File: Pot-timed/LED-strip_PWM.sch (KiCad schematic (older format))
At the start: 14 parts, among them IC1 ATTINY13A-MM, P1 CONN_2, P2 CONN_2, T1 AO3400, U1 MCP1804-SOT23-5

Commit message: Pot-timed: Attiny13 MLF10 (Unobtanium) --> MLF20.
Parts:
- removed IC1: ATTINY13A-MM, QFN/MLF10, symbol ATTINY13A-MM
- added IC1: ATTINY13-M, QFN/MLF20, symbol ATTINY13-M
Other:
- note added: "(MLF-20)"
- note removed: "(MLF-10)"
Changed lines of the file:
@@
-$EndComp
-$Comp
-L ATTINY13A-MM IC1
-U 1 1 519FBED0
-P 1400 800
-F 0 "IC1" H 1500 850 60  0000 C CNN
-F 1 "ATTINY13A-MM" H 2700 50  60  0000 C CNN
-F 2 "QFN/MLF10" H 1700 50  60  0001 C CNN
-F 3 "~" H 1400 800 60  0000 C CNN
-	1    1400 800
-	1    0    0    -1
 $EndComp
 $Comp
@@
 POT1
 Text Notes 2700 775  0    39   ~ 0
-(MLF-10)
+(MLF-20)
 Text Label 950  1300 2    60   ~ 0
 POT2
@@
 Wire Notes Line
 	7300 2000 6000 2000
+$Comp
+L ATTINY13-M IC1
+U 1 1 519FFF57
+P 1400 800
+F 0 "IC1" H 1500 850 60  0000 C CNN
+F 1 "ATTINY13-M" H 2700 50  60  0000 C CNN
+F 2 "QFN/MLF20" H 1700 50  60  0001 C CNN
+F 3 "~" H 1400 800 60  0000 C CNN
+	1    1400 800
+	1    0    0    -1
+$EndComp
 $EndSCHEMATC

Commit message: Pot-timed: Found Attiny13 MLF10 at digikey...
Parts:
- removed IC1: ATTINY13-M, QFN/MLF20, symbol ATTINY13-M
- added IC1: ATTINY13A-MM, QFN/MLF10, symbol ATTINY13A-MM
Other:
- note added: "(MLF-10)"
- note removed: "(MLF-20)"
- moved on the sheet: RV1
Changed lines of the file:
@@
 POT1
 Text Notes 2700 775  0    39   ~ 0
-(MLF-20)
+(MLF-10)
 Text Label 950  1300 2    60   ~ 0
 POT2
@@
 F 3 "~" H 6450 2550 60  0000 C CNN
 	1    6450 2550
-	0    -1   -1   0
+	0    1    1    0
 $EndComp
 $Comp
@@
 	6800 2850 6800 2900
 Connection ~ 6800 2850
-Text Label 6250 2550 2    60   ~ 0
+Text Label 6650 2550 3    60   ~ 0
 POT1
-Text Label 6900 2550 2    60   ~ 0
+Text Label 6900 2550 1    60   ~ 0
 POT2
 Wire Wire Line
 	6900 2550 6950 2550
-Wire Wire Line
-	6250 2550 6300 2550
 Wire Notes Line
 	6000 2000 6000 3000
@@
 	7300 2000 6000 2000
 $Comp
-L ATTINY13-M IC1
-U 1 1 519FFF57
+L ATTINY13A-MM IC1
+U 1 1 51A021E9
 P 1400 800
 F 0 "IC1" H 1500 850 60  0000 C CNN
-F 1 "ATTINY13-M" H 2700 50  60  0000 C CNN
-F 2 "QFN/MLF20" H 1700 50  60  0001 C CNN
+F 1 "ATTINY13A-MM" H 2700 50  60  0000 C CNN
+F 2 "QFN/MLF10" H 1700 50  60  0001 C CNN
 F 3 "~" H 1400 800 60  0000 C CNN
 	1    1400 800
 	1    0    0    -1
 $EndComp
+Wire Wire Line
+	6600 2550 6650 2550
 $EndSCHEMATC

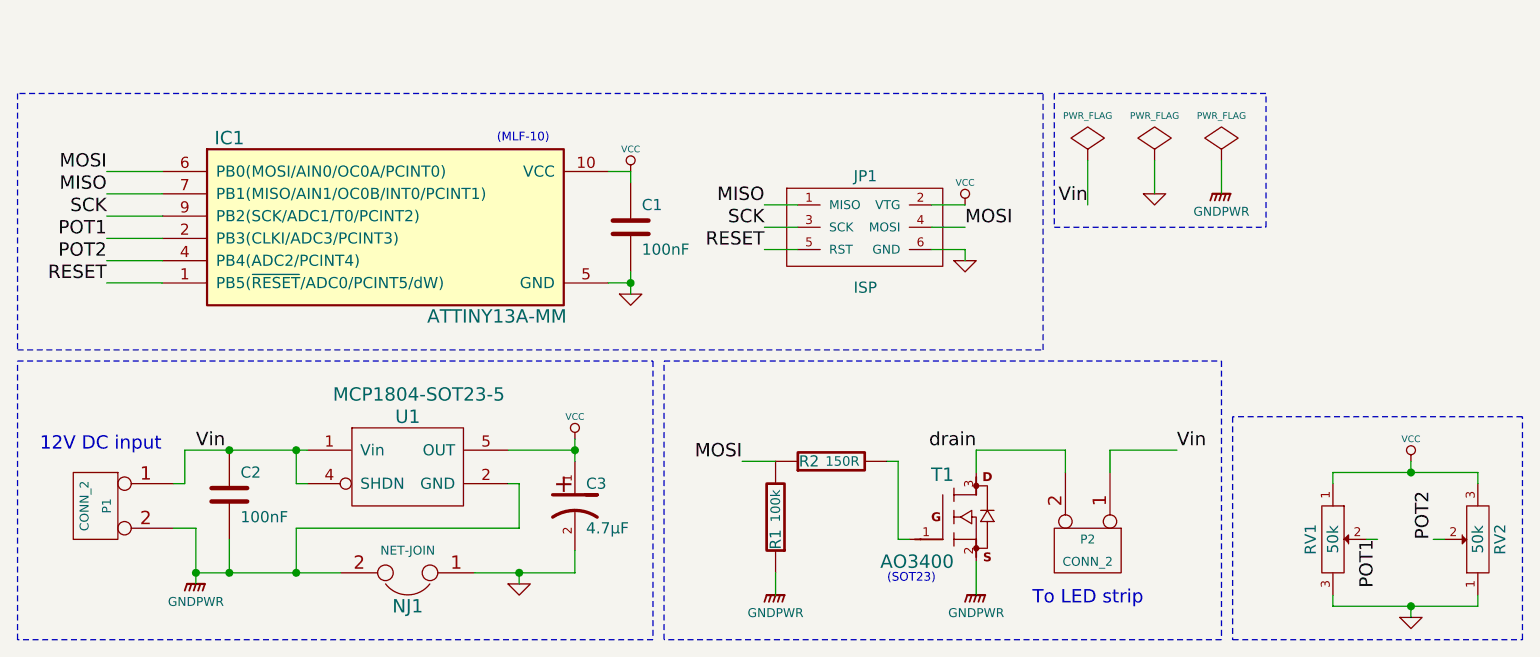
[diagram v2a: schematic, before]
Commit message: Changed to custom attiny13 schematic symbol + footprint.
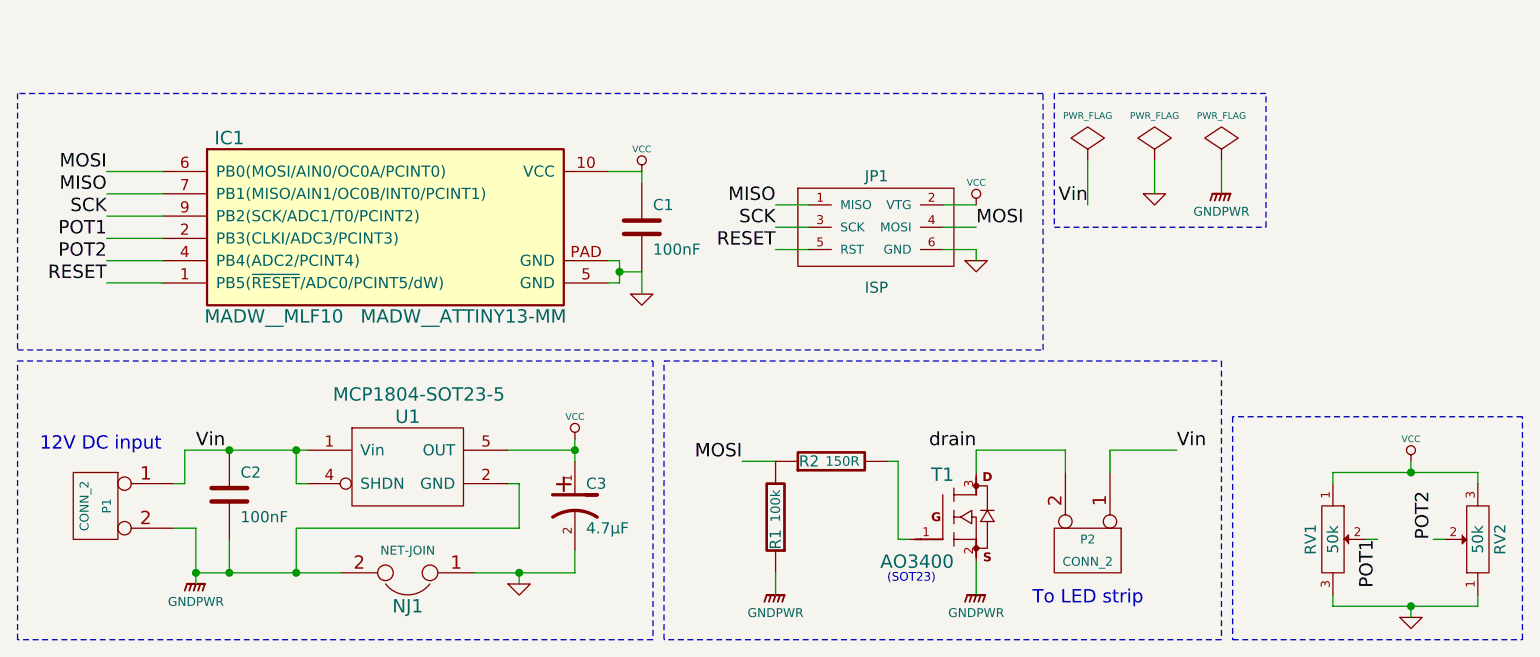
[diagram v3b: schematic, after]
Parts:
- removed IC1: ATTINY13A-MM, QFN/MLF10, symbol ATTINY13A-MM
- added IC1: MADW__ATTINY13-MM, MADW__MLF10, symbol MADW__ATTINY13-MM
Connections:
- net GND: now also IC1.5 (GND), IC1.PAD (GND)
- net MISO: now also IC1.7 (PB1(MISO/AIN1/OC0B/INT0/PCINT1))
- net MOSI: now also IC1.6 (PB0(MOSI/AIN0/OC0A/PCINT0))
- net POT1: now also IC1.2 (PB3(CLKI/ADC3/PCINT3))
- net POT2: now also IC1.4 (PB4(ADC2/PCINT4))
- net RESET: now also IC1.1 (PB5(~RESET~/ADC0/PCINT5/dW))
- net SCK: now also IC1.9 (PB2(SCK/ADC1/T0/PCINT2))
- net VCC: now also IC1.10 (VCC)
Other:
- note removed: "(MLF-10)"
- moved on the sheet: C1, JP1
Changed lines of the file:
@@
-$EndComp
-$Comp
-L C C1
-U 1 1 4F76EBA8
-P 3300 1150
-F 0 "C1" H 3350 1250 50  0000 L CNN
-F 1 "100nF" H 3350 1050 50  0000 L CNN
-F 2 "" H 3300 1150 60  0001 C CNN
-F 3 "" H 3300 1150 60  0001 C CNN
-	1    3300 1150
-	1    0    0    -1
 $EndComp
 $Comp
@@
 L VCC #PWR02
 U 1 1 4F6EE887
-P 3300 900
-F 0 "#PWR02" H 3300 1000 30  0001 C CNN
-F 1 "VCC" H 3300 1000 30  0000 C CNN
-F 2 "" H 3300 900 60  0001 C CNN
-F 3 "" H 3300 900 60  0001 C CNN
-	1    3300 900
+P 3350 900
+F 0 "#PWR02" H 3350 1000 30  0001 C CNN
+F 1 "VCC" H 3350 1000 30  0000 C CNN
+F 2 "" H 3350 900 60  0001 C CNN
+F 3 "" H 3350 900 60  0001 C CNN
+	1    3350 900
 	1    0    0    -1
 $EndComp
@@
 L GND #PWR03
 U 1 1 4F6EE882
-P 3300 1450
-F 0 "#PWR03" H 3300 1450 30  0001 C CNN
-F 1 "GND" H 3300 1380 30  0001 C CNN
-F 2 "" H 3300 1450 60  0001 C CNN
-F 3 "" H 3300 1450 60  0001 C CNN
-	1    3300 1450
+P 3350 1450
+F 0 "#PWR03" H 3350 1450 30  0001 C CNN
+F 1 "GND" H 3350 1380 30  0001 C CNN
+F 2 "" H 3350 1450 60  0001 C CNN
+F 3 "" H 3350 1450 60  0001 C CNN
+	1    3350 1450
 	1    0    0    -1
 $EndComp
@@
 L GND #PWR04
 U 1 1 4F6EE81E
-P 4800 1300
-F 0 "#PWR04" H 4800 1300 30  0001 C CNN
-F 1 "GND" H 4800 1230 30  0001 C CNN
-F 2 "" H 4800 1300 60  0001 C CNN
-F 3 "" H 4800 1300 60  0001 C CNN
-	1    4800 1300
-	1    0    0    -1
-$EndComp
-Text Label 4800 1150 0    60   ~ 0
+P 4850 1300
+F 0 "#PWR04" H 4850 1300 30  0001 C CNN
+F 1 "GND" H 4850 1230 30  0001 C CNN
+F 2 "" H 4850 1300 60  0001 C CNN
+F 3 "" H 4850 1300 60  0001 C CNN
+	1    4850 1300
+	1    0    0    -1
+$EndComp
+Text Label 4850 1150 0    60   ~ 0
 MOSI
 $Comp
 L VCC #PWR05
 U 1 1 4F6EE80A
-P 4800 1050
-F 0 "#PWR05" H 4800 1150 30  0001 C CNN
-F 1 "VCC" H 4800 1150 30  0000 C CNN
-F 2 "" H 4800 1050 60  0001 C CNN
-F 3 "" H 4800 1050 60  0001 C CNN
-	1    4800 1050
-	1    0    0    -1
-$EndComp
-Text Label 3900 1250 2    60   ~ 0
+P 4850 1050
+F 0 "#PWR05" H 4850 1150 30  0001 C CNN
+F 1 "VCC" H 4850 1150 30  0000 C CNN
+F 2 "" H 4850 1050 60  0001 C CNN
+F 3 "" H 4850 1050 60  0001 C CNN
+	1    4850 1050
+	1    0    0    -1
+$EndComp
+Text Label 3950 1250 2    60   ~ 0
 RESET
-Text Label 3900 1150 2    60   ~ 0
+Text Label 3950 1150 2    60   ~ 0
 SCK
-Text Label 3900 1050 2    60   ~ 0
+Text Label 3950 1050 2    60   ~ 0
 MISO
 $Comp
 L MADW__AVR_ISP JP1
 U 1 1 4F6EC6BB
-P 4350 1150
-F 0 "JP1" H 4300 1350 50  0000 L BNN
-F 1 "ISP" H 4300 850 50  0000 L BNN
-F 2 "" H 4350 1150 60  0001 C CNN
-F 3 "" H 4350 1150 60  0001 C CNN
-	1    4350 1150
+P 4400 1150
+F 0 "JP1" H 4350 1350 50  0000 L BNN
+F 1 "ISP" H 4350 850 50  0000 L BNN
+F 2 "" H 4400 1150 60  0001 C CNN
+F 3 "" H 4400 1150 60  0001 C CNN
+	1    4400 1150
 	1    0    0    -1
 $EndComp
@@
 Text Label 950  1200 2    60   ~ 0
 POT1
-Text Notes 2700 775  0    39   ~ 0
-(MLF-10)
 Text Label 950  1300 2    60   ~ 0
 POT2
 Wire Wire Line
-	3300 950  3300 900
-Wire Wire Line
-	3300 900  3200 900
-Wire Wire Line
-	4800 1300 4800 1250
-Wire Wire Line
-	4800 1250 4650 1250
-Wire Wire Line
-	4650 1050 4800 1050
-Wire Wire Line
-	4050 1150 3900 1150
-Wire Wire Line
-	4050 1050 3900 1050
-Wire Wire Line
-	4050 1250 3900 1250
-Wire Wire Line
-	4650 1150 4800 1150
-Wire Wire Line
-	3300 1400 3200 1400
-Wire Wire Line
-	3300 1350 3300 1450
-Connection ~ 3300 1400
+	3200 900  3350 900
+Wire Wire Line
+	4850 1300 4850 1250
+Wire Wire Line
+	4850 1250 4700 1250
+Wire Wire Line
+	4700 1050 4850 1050
+Wire Wire Line
+	4100 1150 3950 1150
+Wire Wire Line
+	4100 1050 3950 1050
+Wire Wire Line
+	4100 1250 3950 1250
+Wire Wire Line
+	4700 1150 4850 1150
 Wire Wire Line
 	4850 2650 4850 2800
@@
 Wire Notes Line
 	7300 2000 6000 2000
-$Comp
-L ATTINY13A-MM IC1
-U 1 1 51A021E9
-P 1400 800
-F 0 "IC1" H 1500 850 60  0000 C CNN
-F 1 "ATTINY13A-MM" H 2700 50  60  0000 C CNN
-F 2 "QFN/MLF10" H 1700 50  60  0001 C CNN
-F 3 "~" H 1400 800 60  0000 C CNN
-	1    1400 800
-	1    0    0    -1
-$EndComp
 Wire Wire Line
 	6600 2550 6650 2550
+$Comp
+L MADW__ATTINY13-MM IC1
+U 1 1 51B1F1AE
+P 2200 1150
+F 0 "IC1" H 1500 1550 60  0000 C CNN
+F 1 "MADW__ATTINY13-MM" H 2550 750 60  0000 C CNN
+F 2 "MADW__MLF10" H 1700 750 60  0000 C CNN
+F 3 "" H 1400 1500 60  0000 C CNN
+	1    2200 1150
+	1    0    0    -1
+$EndComp
+$Comp
+L C C1
+U 1 1 4F76EBA8
+P 3350 1150
+F 0 "C1" H 3400 1250 50  0000 L CNN
+F 1 "100nF" H 3400 1050 50  0000 L CNN
+F 2 "" H 3350 1150 60  0001 C CNN
+F 3 "" H 3350 1150 60  0001 C CNN
+	1    3350 1150
+	1    0    0    -1
+$EndComp
+Wire Wire Line
+	3350 900  3350 950
+Wire Wire Line
+	3350 1350 3350 1450
+Wire Wire Line
+	3200 1300 3250 1300
+Wire Wire Line
+	3250 1300 3250 1400
+Wire Wire Line
+	3250 1400 3200 1400
+Wire Wire Line
+	3250 1350 3350 1350
+Connection ~ 3250 1350
 $EndSCHEMATC

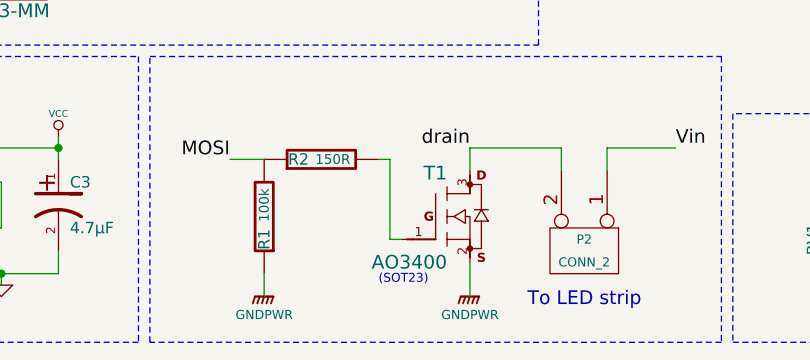
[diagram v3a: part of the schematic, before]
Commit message: Pot-timed (s.b.): added alternative MOSFET to schematic + Rev. update.
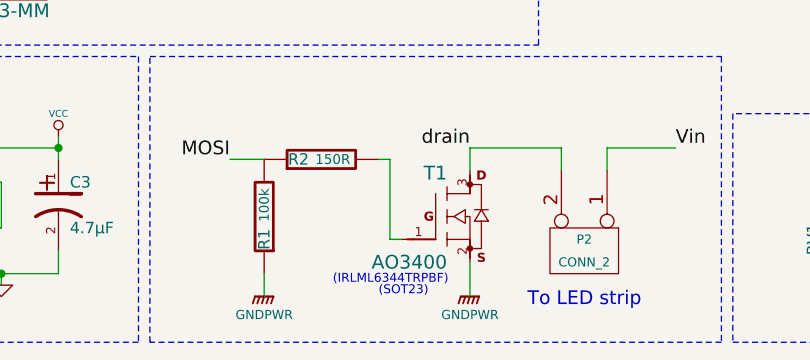
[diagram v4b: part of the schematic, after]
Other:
- note added: "(IRLML6344TRPBF)"
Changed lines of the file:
@@
 Sheet 1 1
 Title "LED-strip_PWM"
-Date "24 May 2013"
-Rev "0.1"
+Date "18 Jul 2013"
+Rev "0.12"
 Comp "2013 - blog.spitzenpfeil.org"
 Comment1 ""
@@
 	1    0    0    -1
 $EndComp
-Text Notes 4450 2750 0    39   ~ 0
+Text Notes 4450 2800 0    39   ~ 0
 (SOT23)
 Text Label 950  1200 2    60   ~ 0
@@
 	3250 1350 3350 1350
 Connection ~ 3250 1350
+Text Notes 4250 2750 0    39   ~ 0
+(IRLML6344TRPBF)
 $EndSCHEMATC

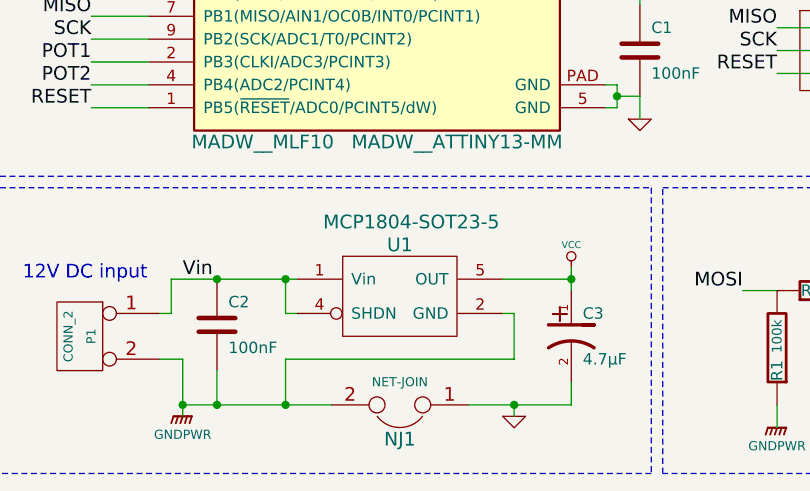
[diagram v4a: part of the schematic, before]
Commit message: Replaced MCP1804 with AP2204K-3.3TRG1 [TS5205CX533].
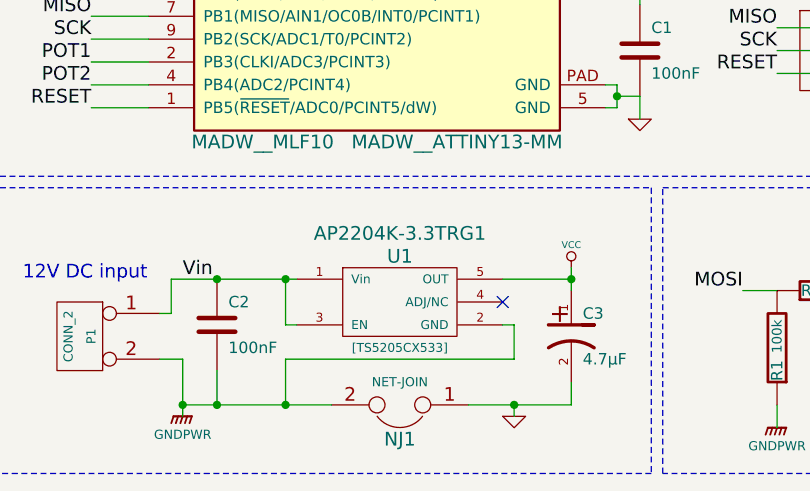
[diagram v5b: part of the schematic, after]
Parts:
- removed U1: MCP1804-SOT23-5, symbol MADW__MCP1804-SOT23-5
- added U1: AP2204K-3.3TRG1, my_parts:MADW__SOT23-5, symbol MADW__AP2204K-SOT23-5
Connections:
- net GNDPWR: now also U1.2 (GND)
- net VCC: now also U1.5 (OUT)
- net Vin: now also U1.1 (Vin), U1.3 (EN)
- no-connect marks 0 -> 1
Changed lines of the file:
@@
 EESchema Schematic File Version 2
 LIBS:my_parts
-LIBS:power
-LIBS:device
-LIBS:transistors
-LIBS:conn
-LIBS:linear
-LIBS:regul
-LIBS:74xx
-LIBS:cmos4000
-LIBS:adc-dac
-LIBS:memory
-LIBS:xilinx
-LIBS:special
-LIBS:microcontrollers
-LIBS:dsp
-LIBS:microchip
-LIBS:analog_switches
-LIBS:motorola
-LIBS:texas
-LIBS:intel
-LIBS:audio
-LIBS:interface
-LIBS:digital-audio
-LIBS:philips
-LIBS:display
-LIBS:cypress
-LIBS:siliconi
-LIBS:opto
-LIBS:atmel
-LIBS:contrib
-LIBS:valves
-LIBS:murata-resonators
 LIBS:LED-strip_PWM-cache
-EELAYER 24 0
+EELAYER 25 0
 EELAYER END
 $Descr User 8268 5906
@@
 Sheet 1 1
 Title "LED-strip_PWM"
-Date "18 Jul 2013"
-Rev "0.12"
+Date "Fri 03 Apr 2015"
+Rev "0.13"
 Comp "2013 - blog.spitzenpfeil.org"
 Comment1 ""
@@
 $EndComp
 $Comp
-L MADW__MCP1804-SOT23-5 U1
-U 1 1 50ED7AA4
-P 2300 2300
-F 0 "U1" H 2300 2600 60  0000 C CNN
-F 1 "MCP1804-SOT23-5" H 2350 2700 60  0000 C CNN
-F 2 "" H 2300 2300 60  0001 C CNN
-F 3 "" H 2300 2300 60  0001 C CNN
-	1    2300 2300
-	1    0    0    -1
-$EndComp
-$Comp
 L GND #PWR011
 U 1 1 50B21224
@@
 Wire Wire Line
 	5650 850  5650 1000
-Wire Wire Line
-	1800 2300 1850 2300
 Connection ~ 1800 2150
 Wire Wire Line
-	1800 2150 1800 2300
-Wire Wire Line
-	2750 2300 2800 2300
+	1800 2150 1800 2350
 Wire Wire Line
 	2600 2700 3050 2700
@@
 Wire Wire Line
 	1800 2500 2800 2500
-Wire Wire Line
-	2800 2500 2800 2300
 Connection ~ 1800 2700
 Wire Wire Line
@@
 Text Notes 4250 2750 0    39   ~ 0
 (IRLML6344TRPBF)
+$Comp
+L MADW__AP2204K-SOT23-5 U1
+U 1 1 551DC2CC
+P 2300 2250
+F 0 "U1" H 2300 2450 60  0000 C CNN
+F 1 "AP2204K-3.3TRG1" H 2300 2550 60  0000 C CNN
+F 2 "my_parts:MADW__SOT23-5" H 2300 2200 60  0001 C CNN
+F 3 "" H 2300 2200 60  0000 C CNN
+F 4 "[TS5205CX533]" H 2300 2050 39  0000 C CNN "Alternative part"
+	1    2300 2250
+	1    0    0    -1
+$EndComp
+Wire Wire Line
+	1800 2350 1850 2350
+NoConn ~ 2750 2250
+Wire Wire Line
+	2750 2350 2800 2350
+Wire Wire Line
+	2800 2350 2800 2500
 $EndSCHEMATC
